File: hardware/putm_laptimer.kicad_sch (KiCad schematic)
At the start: 45 parts, among them J1 Conn_01x22, J10 Conn_01x07, J11 Conn_01x09, J12 Conn_01x01, J13 Conn_01x01, J14 Conn_01x01, J15 Conn_01x01, J16 2601-1103, J2 Conn_01x22, J3 Conn_01x22, J4 Conn_01x22, J5 2601-3109, J6 Conn_02x05_Odd_Even, J7 2601-1102, J8 2601-3109, J9 Conn_01x07

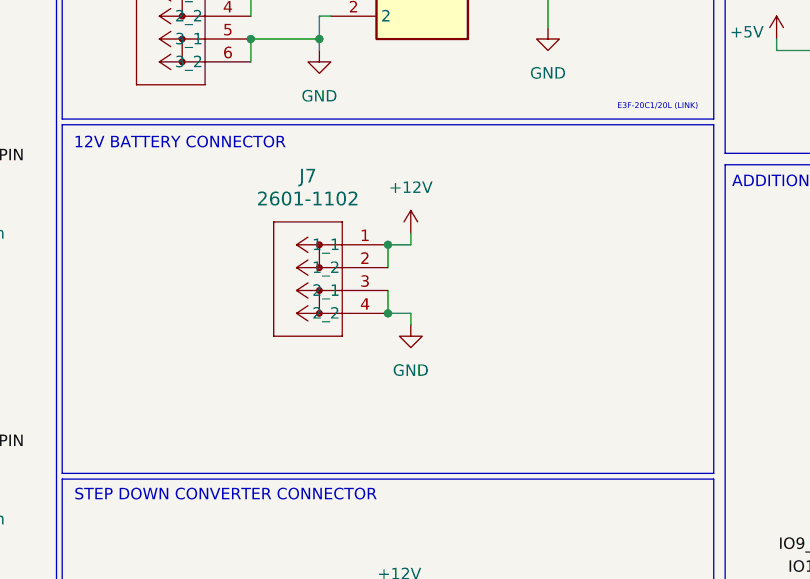
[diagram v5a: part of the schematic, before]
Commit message: Added pwr flags on battery connector and fixed wago connector footprint malformed courtyard
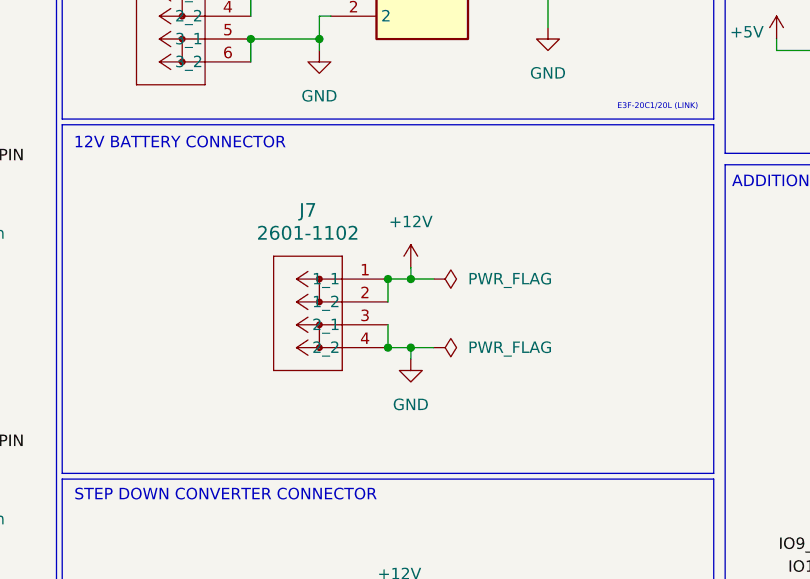
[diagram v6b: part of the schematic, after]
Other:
- moved on the sheet: J7
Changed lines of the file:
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@@
 	)
 	(junction
-		(at 171.45 104.14)
+		(at 171.45 107.95)
 		(diameter 0)
 		(color 0 0 0 0)
@@
 	)
 	(junction
-		(at 171.45 111.76)
+		(at 171.45 115.57)
 		(diameter 0)
 		(color 0 0 0 0)
@@
 	)
 	(junction
+		(at 173.99 115.57)
+		(diameter 0)
+		(color 0 0 0 0)
+	)
+	(junction
 		(at 30.48 54.61)
 		(diameter 0)
@@
 	)
 	(junction
+		(at 173.99 107.95)
+		(diameter 0)
+		(color 0 0 0 0)
+	)
+	(junction
 		(at 189.23 76.2)
 		(diameter 0)
@@
 	(wire
 		(pts
-			(xy 171.45 104.14) (xy 171.45 106.68)
+			(xy 171.45 107.95) (xy 171.45 110.49)
 		)
 		(stroke
@@
 	(wire
 		(pts
+			(xy 173.99 115.57) (xy 176.53 115.57)
+		)
+		(stroke
+			(width 0)
+			(type default)
+		)
+	)
+	(wire
+		(pts
 			(xy 120.65 52.07) (xy 120.65 53.34)
 		)
@@
 	(wire
 		(pts
-			(xy 171.45 111.76) (xy 173.99 111.76)
+			(xy 171.45 115.57) (xy 173.99 115.57)
 		)
 		(stroke
@@
 	(wire
 		(pts
-			(xy 171.45 109.22) (xy 171.45 111.76)
+			(xy 171.45 113.03) (xy 171.45 115.57)
 		)
 		(stroke
@@
 	(wire
 		(pts
-			(xy 173.99 102.87) (xy 173.99 104.14)
+			(xy 173.99 106.68) (xy 173.99 107.95)
 		)
 		(stroke
@@
 	(wire
 		(pts
+			(xy 173.99 107.95) (xy 176.53 107.95)
+		)
+		(stroke
+			(width 0)
+			(type default)
+		)
+	)
+	(wire
+		(pts
 			(xy 261.62 156.21) (xy 264.16 156.21)
 		)
@@
 	(wire
 		(pts
-			(xy 173.99 111.76) (xy 173.99 113.03)
+			(xy 173.99 115.57) (xy 173.99 116.84)
 		)
 		(stroke
@@
 	(wire
 		(pts
-			(xy 171.45 104.14) (xy 173.99 104.14)
+			(xy 171.45 107.95) (xy 173.99 107.95)
 		)
 		(stroke
@@
 	(symbol
 		(lib_id "power:GND")
-		(at 173.99 113.03 0)
+		(at 173.99 116.84 0)
 		(unit 1)
 		(exclude_from_sim no)
@@
 		(fields_autoplaced yes)
 		(property "Reference" "#PWR014"
-			(at 173.99 119.38 0)
+			(at 173.99 123.19 0)
 			(effects
 				(font
@@
 		)
 		(property "Value" "GND"
-			(at 173.99 118.11 0)
+			(at 173.99 121.92 0)
 			(effects
 				(font
@@
 		)
 		(property "Footprint" ""
-			(at 173.99 113.03 0)
+			(at 173.99 116.84 0)
 			(effects
 				(font
@@
 		)
 		(property "Datasheet" ""
-			(at 173.99 113.03 0)
+			(at 173.99 116.84 0)
 			(effects
 				(font
@@
 		)
 		(property "Description" "Power symbol creates a global label with name \"GND\" , ground"
-			(at 173.99 113.03 0)
+			(at 173.99 116.84 0)
 			(effects
 				(font
@@
 	(symbol
 		(lib_id "2026-02-04_12-17-39:2601-1102")
-		(at 171.45 104.14 0)
+		(at 171.45 107.95 0)
 		(mirror y)
 		(unit 1)
@@
 		(fields_autoplaced yes)
 		(property "Reference" "J7"
-			(at 162.56 96.52 0)
+			(at 162.56 100.33 0)
 			(effects
 				(font
@@
 		)
 		(property "Value" "2601-1102"
-			(at 162.56 99.06 0)
+			(at 162.56 102.87 0)
 			(effects
 				(font
@@
 		)
 		(property "Footprint" "CONN2_2601-1102_WAG"
-			(at 171.45 104.14 0)
+			(at 171.45 107.95 0)
 			(effects
 				(font
@@
 		)
 		(property "Datasheet" "https://www.wago.com/pl/z%C5%82%C4%85czki-do-p%C5%82ytek-drukowanych/z%C5%82%C4%85cze-do%C2%A0pcb/p/2601-1102#details"
-			(at 171.45 104.14 0)
+			(at 171.45 107.95 0)
 			(effects
 				(font
@@
 		)
 		(property "Description" ""
-			(at 171.45 104.14 0)
+			(at 171.45 107.95 0)
 			(effects
 				(font
@@
 	)
 	(symbol
+		(lib_id "power:PWR_FLAG")
+		(at 176.53 115.57 270)
+		(unit 1)
+		(exclude_from_sim no)
+		(in_bom yes)
+		(on_board yes)
+		(dnp no)
+		(fields_autoplaced yes)
+		(property "Reference" "#FLG02"
+			(at 178.435 115.57 0)
+			(effects
+				(font
+					(size 1.27 1.27)
+				)
+				(hide yes)
+			)
+		)
+		(property "Value" "PWR_FLAG"
+			(at 180.34 115.5699 90)
+			(effects
+				(font
+					(size 1.27 1.27)
+				)
+				(justify left)
+			)
+		)
+		(property "Footprint" ""
+			(at 176.53 115.57 0)
+			(effects
+				(font
+					(size 1.27 1.27)
+				)
+				(hide yes)
+			)
+		)
+		(property "Datasheet" "~"
+			(at 176.53 115.57 0)
+			(effects
+				(font
+					(size 1.27 1.27)
+				)
+				(hide yes)
+			)
+		)
+		(property "Description" "Special symbol for telling ERC where power comes from"
+			(at 176.53 115.57 0)
+			(effects
+				(font
+					(size 1.27 1.27)
+				)
+				(hide yes)
+			)
+		)
+		(pin "1"
+		)
+		(instances
+			(project ""
+				(path "/b652b05a-4e3d-4ad1-b032-18886abe7d45"
+					(reference "#FLG02")
+					(unit 1)
+				)
+			)
+		)
+	)
+	(symbol
 		(lib_id "power:+3V3")
 		(at 231.14 101.6 0)
@@
 	)
 	(symbol
+		(lib_id "power:PWR_FLAG")
+		(at 176.53 107.95 270)
+		(unit 1)
+		(exclude_from_sim no)
+		(in_bom yes)
+		(on_board yes)
+		(dnp no)
+		(fields_autoplaced yes)
+		(property "Reference" "#FLG01"
+			(at 178.435 107.95 0)
+			(effects
+				(font
+					(size 1.27 1.27)
+				)
+				(hide yes)
+			)
+		)
+		(property "Value" "PWR_FLAG"
+			(at 180.34 107.9499 90)
+			(effects
+				(font
+					(size 1.27 1.27)
+				)
+				(justify left)
+			)
+		)
+		(property "Footprint" ""
+			(at 176.53 107.95 0)
+			(effects
+				(font
+					(size 1.27 1.27)
+				)
+				(hide yes)
+			)
+		)
+		(property "Datasheet" "~"
+			(at 176.53 107.95 0)
+			(effects
+				(font
+					(size 1.27 1.27)
+				)
+				(hide yes)
+			)
+		)
+		(property "Description" "Special symbol for telling ERC where power comes from"
+			(at 176.53 107.95 0)
+			(effects
+				(font
+					(size 1.27 1.27)
+				)
+				(hide yes)
+			)
+		)
+		(pin "1"
+		)
+		(instances
+			(project ""
+				(path "/b652b05a-4e3d-4ad1-b032-18886abe7d45"
+					(reference "#FLG01")
+					(unit 1)
+				)
+			)
+		)
+	)
+	(symbol
 		(lib_id "2026-02-04_11-25-15:2601-1103")
 		(at 156.21 71.12 0)
@@
 	(symbol
 		(lib_id "power:+12V")
-		(at 173.99 102.87 0)
+		(at 173.99 106.68 0)
 		(unit 1)
 		(exclude_from_sim no)
@@
 		(fields_autoplaced yes)
 		(property "Reference" "#PWR010"
-			(at 173.99 106.68 0)
+			(at 173.99 110.49 0)
 			(effects
 				(font
@@
 		)
 		(property "Value" "+12V"
-			(at 173.99 97.79 0)
+			(at 173.99 101.6 0)
 			(effects
 				(font
@@
 		)
 		(property "Footprint" ""
-			(at 173.99 102.87 0)
+			(at 173.99 106.68 0)
 			(effects
 				(font
@@
 		)
 		(property "Datasheet" ""
-			(at 173.99 102.87 0)
+			(at 173.99 106.68 0)
 			(effects
 				(font
@@
 		)
 		(property "Description" "Power symbol creates a global label with name \"+12V\""
-			(at 173.99 102.87 0)
+			(at 173.99 106.68 0)
 			(effects
 				(font

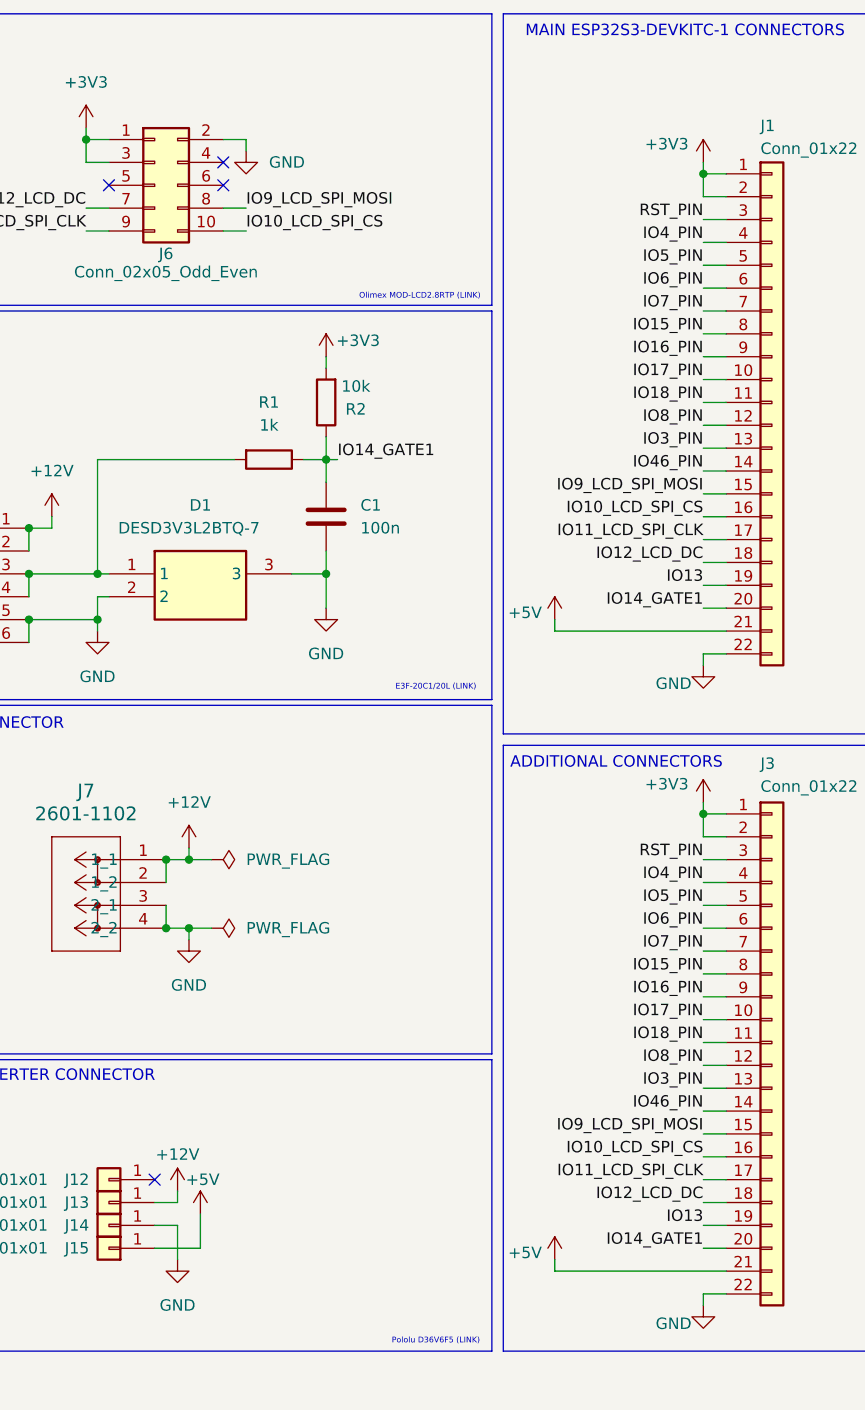
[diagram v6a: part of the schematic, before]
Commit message: Added reverse polarity protection diode, deleted unused footprints
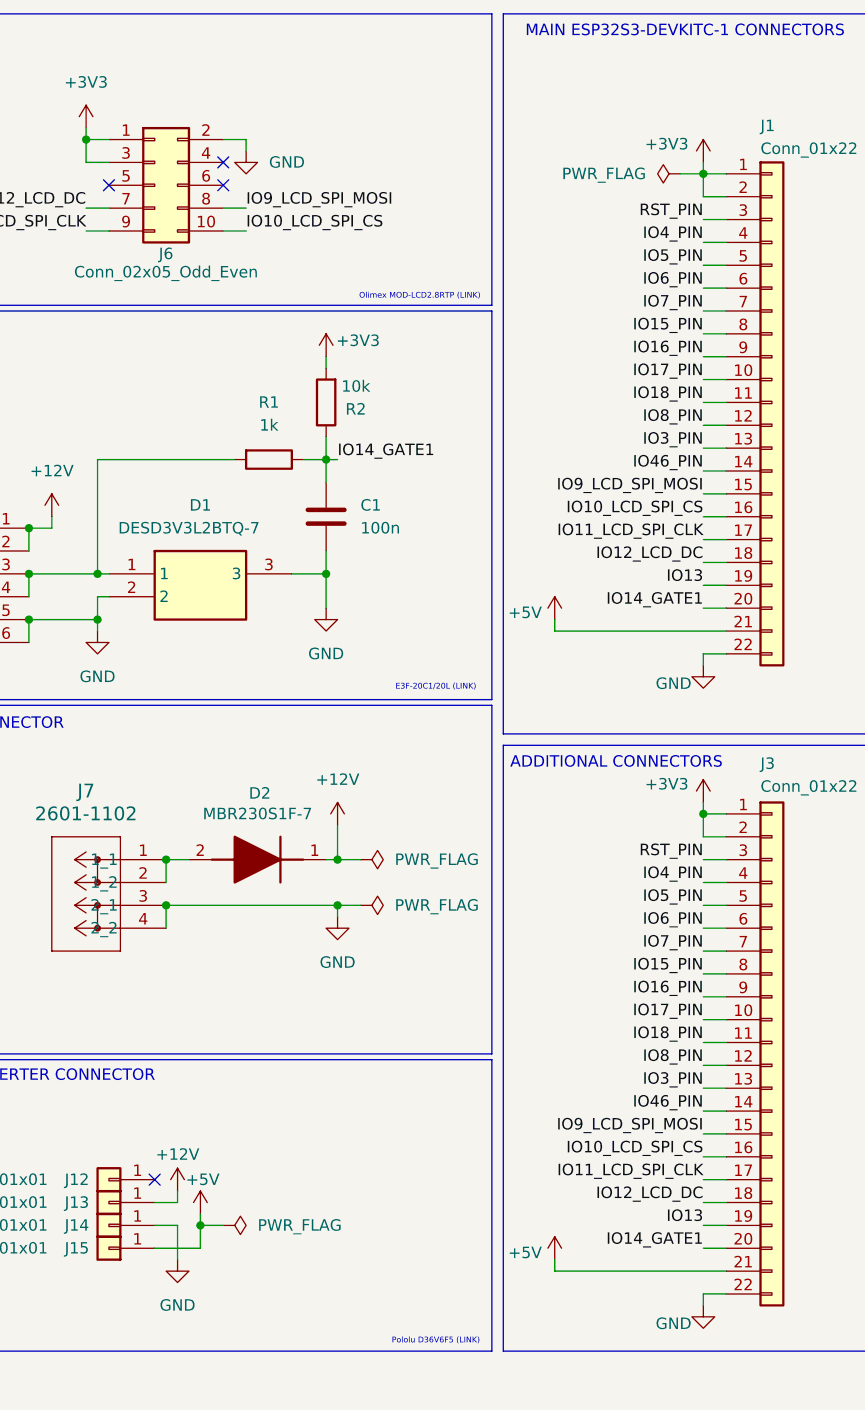
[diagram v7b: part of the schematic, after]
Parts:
- added D2: MBR230S1F-7, SODFL3518X115N, symbol MBR230S1F-7:MBR230S1F-7
- J16: footprint CONN3_2601-1103_WAG -> Footprint:CONN3_2601-1103_WAG
- J5, J8: footprint CONN9_2601-3109_WAG -> Footprint:CONN9_2601-3109_WAG
- J7: footprint CONN2_2601-1102_WAG -> Footprint:CONN2_2601-1102_WAG
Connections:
- net +12V: now also D2.1 (K); no longer J7.1 (1_1), J7.2 (1_2)
- new net: D2.2 (A), J7.1 (1_1), J7.2 (1_2)

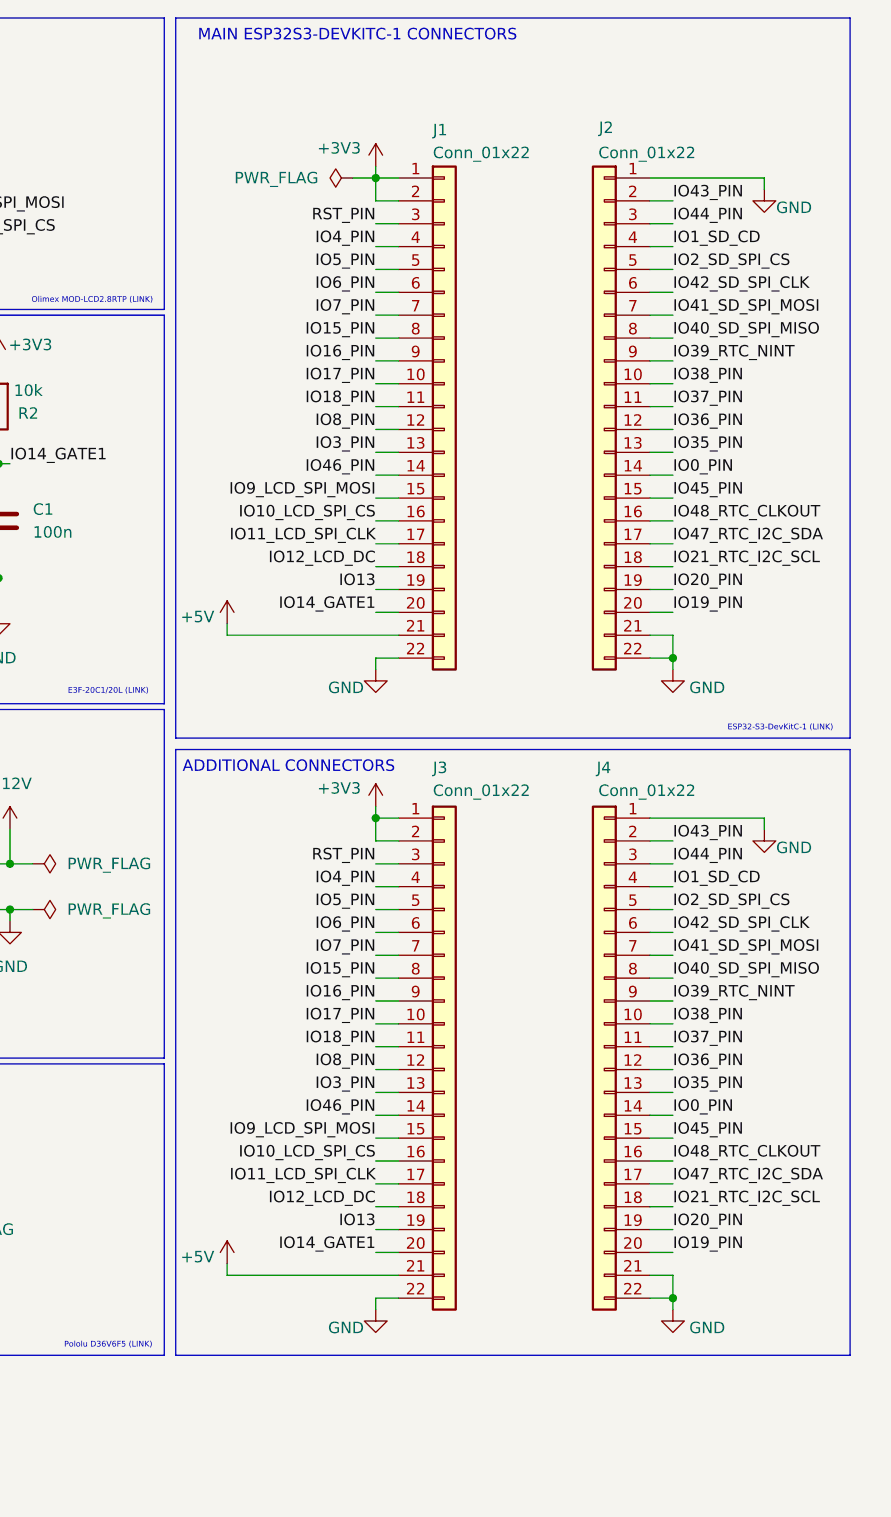
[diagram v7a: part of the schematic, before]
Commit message: Changed esp32 connector
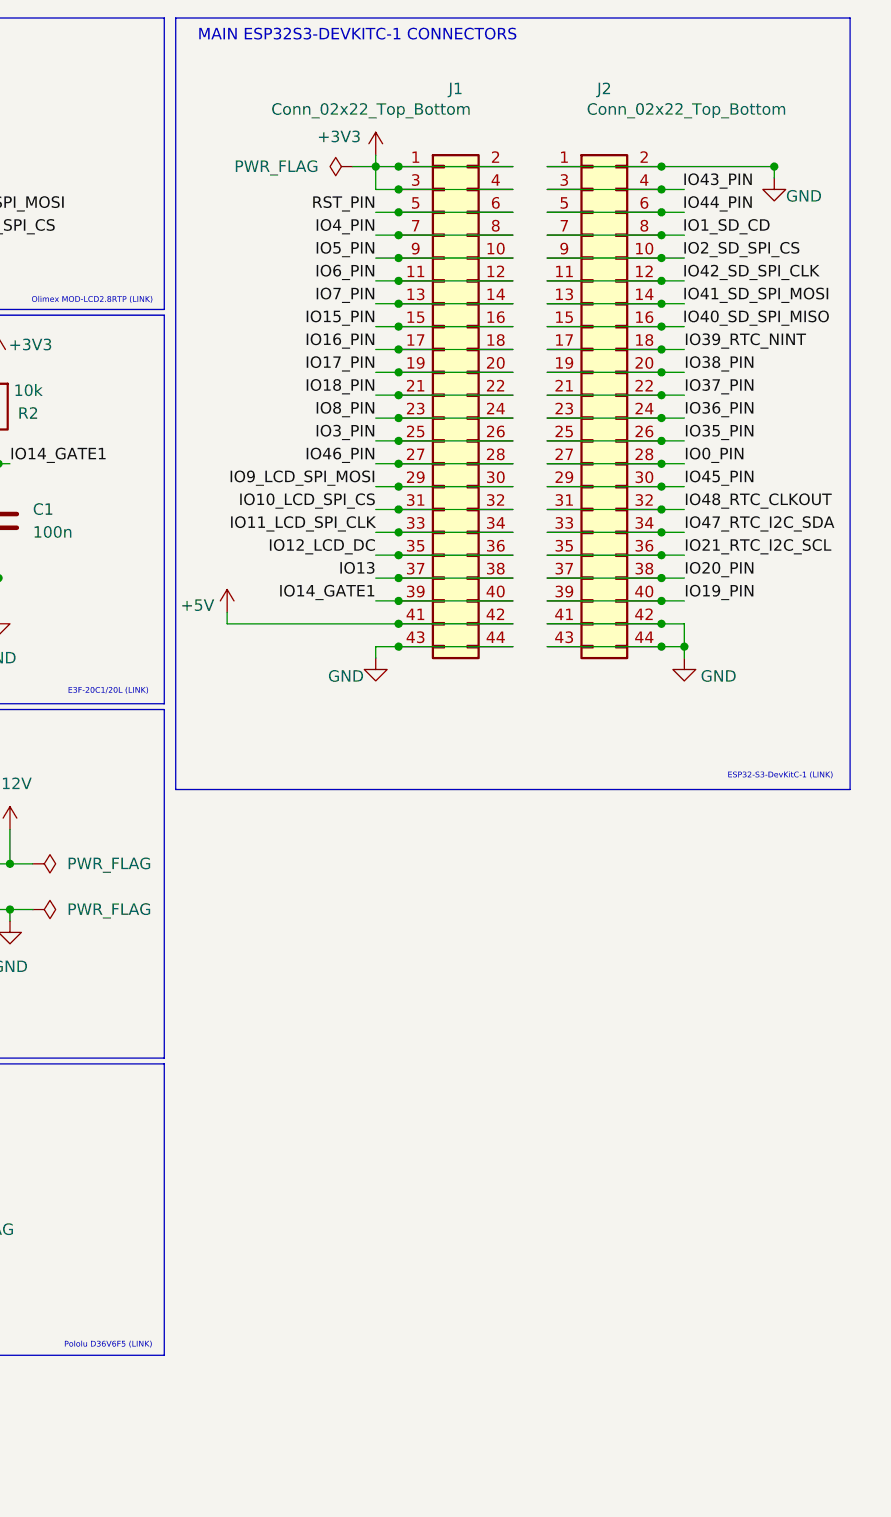
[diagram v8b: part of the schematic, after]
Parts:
- removed J1, J2, J3, J4: Conn_01x22, Connector_PinSocket_2.54mm:PinSocket_1x22_P2.54mm_Vertical, symbol Connector_Generic:Conn_01x22
- added J1, J2: Conn_02x22_Top_Bottom, Connector_PinSocket_2.54mm:PinSocket_2x22_P2.54mm_Vertical, symbol Connector_Generic:Conn_02x22_Odd_Even
- D1: Mouser Part Number (none) -> 621-DESD3V3L2BTQ-7
- D2: footprint SODFL3518X115N -> Footprint:SODFL3518X115N
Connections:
- net +3V3: now also J1.1 (Pin_1), J1.2 (Pin_2), J1.3 (Pin_3), J1.4 (Pin_4)
- net +5V: now also J1.41 (Pin_41), J1.42 (Pin_42)
- net GND: now also J1.43 (Pin_43), J1.44 (Pin_44), J2.1 (Pin_1), J2.2 (Pin_2), J2.41 (Pin_41), J2.42 (Pin_42), J2.43 (Pin_43), J2.44 (Pin_44)
- net IO0_PIN: now also J2.27 (Pin_27), J2.28 (Pin_28)
- net IO10_LCD_SPI_CS: now also J1.31 (Pin_31), J1.32 (Pin_32)
- net IO11_LCD_SPI_CLK: now also J1.33 (Pin_33), J1.34 (Pin_34)
- net IO12_LCD_DC: now also J1.35 (Pin_35), J1.36 (Pin_36)
- net IO13: now also J1.37 (Pin_37), J1.38 (Pin_38)
- net IO14_GATE1: now also J1.39 (Pin_39), J1.40 (Pin_40)
- net IO15_PIN: now also J1.15 (Pin_15), J1.16 (Pin_16)
- net IO16_PIN: now also J1.17 (Pin_17), J1.18 (Pin_18)
- net IO17_PIN: now also J1.19 (Pin_19), J1.20 (Pin_20)
- net IO18_PIN: now also J1.21 (Pin_21), J1.22 (Pin_22)
- net IO19_PIN: now also J2.39 (Pin_39), J2.40 (Pin_40)
- net IO1_SD_CD: now also J2.7 (Pin_7), J2.8 (Pin_8)
- net IO20_PIN: now also J2.37 (Pin_37), J2.38 (Pin_38)
- net IO21_RTC_I2C_SCL: now also J2.35 (Pin_35), J2.36 (Pin_36)
- net IO2_SD_SPI_CS: now also J2.10 (Pin_10), J2.9 (Pin_9)
- net IO35_PIN: now also J2.25 (Pin_25), J2.26 (Pin_26)
- net IO36_PIN: now also J2.23 (Pin_23), J2.24 (Pin_24)
- net IO37_PIN: now also J2.21 (Pin_21), J2.22 (Pin_22)
- net IO38_PIN: now also J2.19 (Pin_19), J2.20 (Pin_20)
- net IO39_RTC_NINT: now also J2.17 (Pin_17), J2.18 (Pin_18)
- net IO3_PIN: now also J1.25 (Pin_25), J1.26 (Pin_26)
- net IO40_SD_SPI_MISO: now also J2.15 (Pin_15), J2.16 (Pin_16)
- net IO41_SD_SPI_MOSI: now also J2.13 (Pin_13), J2.14 (Pin_14)
- net IO42_SD_SPI_CLK: now also J2.11 (Pin_11), J2.12 (Pin_12)
- net IO43_PIN: now also J2.3 (Pin_3), J2.4 (Pin_4)
- net IO44_PIN: now also J2.5 (Pin_5), J2.6 (Pin_6)
- net IO45_PIN: now also J2.29 (Pin_29), J2.30 (Pin_30)
- net IO46_PIN: now also J1.27 (Pin_27), J1.28 (Pin_28)
- net IO47_RTC_I2C_SDA: now also J2.33 (Pin_33), J2.34 (Pin_34)
- net IO48_RTC_CLKOUT: now also J2.31 (Pin_31), J2.32 (Pin_32)
- net IO4_PIN: now also J1.7 (Pin_7), J1.8 (Pin_8)
- net IO5_PIN: now also J1.10 (Pin_10), J1.9 (Pin_9)
- net IO6_PIN: now also J1.11 (Pin_11), J1.12 (Pin_12)
- net IO7_PIN: now also J1.13 (Pin_13), J1.14 (Pin_14)
- net IO8_PIN: now also J1.23 (Pin_23), J1.24 (Pin_24)
- net IO9_LCD_SPI_MOSI: now also J1.29 (Pin_29), J1.30 (Pin_30)
- net RST_PIN: now also J1.5 (Pin_5), J1.6 (Pin_6)
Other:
- note removed: "ADDITIONAL CONNECTORS"
